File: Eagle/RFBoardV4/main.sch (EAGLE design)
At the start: 27 parts, among them Q1 8/16/20MHz, Q2 TIP41C, U1 ATMEGA328

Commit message: Added smaller mosfet - WIP
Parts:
- added Q3: (no value), transistors:2N7002_SOT23
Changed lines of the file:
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@@
 <part name="R4" library="SparkFun" deviceset="RESISTOR" device="0603-RES" value="10K"/>
 <part name="GND11" library="SparkFun" deviceset="GND" device=""/>
+<part name="Q3" library="transistors" deviceset="2N700*" device="_SOT23" technology="2"/>
 </parts>
 <sheets>
@@
 <instance part="R4" gate="G$1" x="167.64" y="172.72" rot="R180"/>
 <instance part="GND11" gate="1" x="157.48" y="175.26" rot="R180"/>
+<instance part="Q3" gate="G$1" x="93.98" y="187.96"/>
 </instances>
 <busses>

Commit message: WIP
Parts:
- removed Q2: TIP41C, transistor-power:TIP41C
- added BATMIN1, BATPLUS1: (no value), pinhead:PINHD-1X1
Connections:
- removed net SCREW_PWR: JP4.2, Q2.E
- new net SCREW_GND: JP4.1, Q3.S
- net D5: now also Q3.G; no longer Q2.B
- net GND: now also BATMIN1.1, Q3.D; no longer JP4.1
- net VCC: now also BATPLUS1.1, JP4.2; no longer Q2.C
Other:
- moved on the sheet: Q3
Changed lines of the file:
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@@
 <class number="0" name="default" width="0.1524" drill="0">
 </class>
-<class number="1" name="vcc" width="0.1524" drill="0">
+<class number="1" name="vcc" width="0.4064" drill="0">
+</class>
+<class number="2" name="GND" width="0.4064" drill="0">
 </class>
 </classes>
@@
 <part name="R3" library="SparkFun" deviceset="RESISTOR" device="0603-RES" value="10K"/>
 <part name="JP4" library="SparkFun-Connectors" deviceset="M03" device="SCREW"/>
-<part name="Q2" library="transistor-power" deviceset="TIP41C" device=""/>
 <part name="P+5" library="SparkFun" deviceset="3.3V" device="" value="VCC"/>
 <part name="GND10" library="SparkFun" deviceset="GND" device=""/>
@@
 <part name="GND11" library="SparkFun" deviceset="GND" device=""/>
 <part name="Q3" library="transistors" deviceset="2N700*" device="_SOT23" technology="2"/>
+<part name="BATMIN1" library="pinhead" deviceset="PINHD-1X1" device=""/>
+<part name="BATPLUS1" library="pinhead" deviceset="PINHD-1X1" device=""/>
+<part name="P+6" library="SparkFun" deviceset="3.3V" device="" value="VCC"/>
+<part name="GND12" library="SparkFun" deviceset="GND" device=""/>
 </parts>
 <sheets>
@@
 <instance part="R3" gate="G$1" x="30.48" y="106.68" rot="R90"/>
 <instance part="JP4" gate="G$1" x="220.98" y="187.96" rot="R180"/>
-<instance part="Q2" gate="1" x="177.8" y="185.42" rot="R90"/>
-<instance part="P+5" gate="G$1" x="165.1" y="187.96" rot="R90"/>
-<instance part="GND10" gate="1" x="200.66" y="193.04" rot="R180"/>
+<instance part="P+5" gate="G$1" x="205.74" y="187.96" rot="R90"/>
+<instance part="GND10" gate="1" x="162.56" y="193.04" rot="R180"/>
 <instance part="R4" gate="G$1" x="167.64" y="172.72" rot="R180"/>
-<instance part="GND11" gate="1" x="157.48" y="175.26" rot="R180"/>
-<instance part="Q3" gate="G$1" x="93.98" y="187.96"/>
+<instance part="GND11" gate="1" x="154.94" y="175.26" rot="R180"/>
+<instance part="Q3" gate="G$1" x="177.8" y="190.5" rot="R90"/>
+<instance part="BATMIN1" gate="G$1" x="20.32" y="154.94"/>
+<instance part="BATPLUS1" gate="G$1" x="20.32" y="170.18"/>
+<instance part="P+6" gate="G$1" x="25.4" y="170.18" rot="R270"/>
+<instance part="GND12" gate="1" x="17.78" y="147.32"/>
 </instances>
 <busses>
@@
 </segment>
 <segment>
-<pinref part="JP4" gate="G$1" pin="1"/>
-<pinref part="GND10" gate="1" pin="GND"/>
-<wire x1="213.36" y1="190.5" x2="200.66" y2="190.5" width="0.1524" layer="91"/>
-</segment>
-<segment>
 <pinref part="R4" gate="G$1" pin="2"/>
 <pinref part="GND11" gate="1" pin="GND"/>
-<wire x1="162.56" y1="172.72" x2="157.48" y2="172.72" width="0.1524" layer="91"/>
+<wire x1="162.56" y1="172.72" x2="154.94" y2="172.72" width="0.1524" layer="91"/>
+</segment>
+<segment>
+<pinref part="Q3" gate="G$1" pin="D"/>
+<pinref part="GND10" gate="1" pin="GND"/>
+<wire x1="167.64" y1="190.5" x2="162.56" y2="190.5" width="0.1524" layer="91"/>
+</segment>
+<segment>
+<pinref part="BATMIN1" gate="G$1" pin="1"/>
+<pinref part="GND12" gate="1" pin="GND"/>
+<wire x1="17.78" y1="154.94" x2="17.78" y2="149.86" width="0.1524" layer="91"/>
 </segment>
 </net>
@@
 </segment>
 <segment>
-<pinref part="Q2" gate="1" pin="C"/>
+<pinref part="JP4" gate="G$1" pin="2"/>
 <pinref part="P+5" gate="G$1" pin="3.3V"/>
-<wire x1="172.72" y1="187.96" x2="165.1" y2="187.96" width="0.1524" layer="91"/>
+<wire x1="213.36" y1="187.96" x2="205.74" y2="187.96" width="0.1524" layer="91"/>
+</segment>
+<segment>
+<pinref part="BATPLUS1" gate="G$1" pin="1"/>
+<pinref part="P+6" gate="G$1" pin="3.3V"/>
+<wire x1="17.78" y1="170.18" x2="25.4" y2="170.18" width="0.1524" layer="91"/>
 </segment>
 </net>
@@
 <pinref part="U1" gate="G$1" pin="PD5(T1)"/>
 <wire x1="195.58" y1="119.38" x2="208.28" y2="119.38" width="0.1524" layer="91"/>
-<pinref part="Q2" gate="1" pin="B"/>
-<wire x1="177.8" y1="182.88" x2="177.8" y2="172.72" width="0.1524" layer="91"/>
-<wire x1="177.8" y1="172.72" x2="177.8" y2="160.02" width="0.1524" layer="91"/>
-<wire x1="177.8" y1="160.02" x2="208.28" y2="160.02" width="0.1524" layer="91"/>
+<wire x1="180.34" y1="172.72" x2="180.34" y2="160.02" width="0.1524" layer="91"/>
+<wire x1="180.34" y1="160.02" x2="208.28" y2="160.02" width="0.1524" layer="91"/>
 <wire x1="208.28" y1="160.02" x2="208.28" y2="119.38" width="0.1524" layer="91"/>
-<junction x="177.8" y="172.72"/>
 <pinref part="R4" gate="G$1" pin="1"/>
-<wire x1="172.72" y1="172.72" x2="177.8" y2="172.72" width="0.1524" layer="91"/>
+<wire x1="172.72" y1="172.72" x2="180.34" y2="172.72" width="0.1524" layer="91"/>
+<pinref part="Q3" gate="G$1" pin="G"/>
+<wire x1="180.34" y1="180.34" x2="180.34" y2="172.72" width="0.1524" layer="91"/>
+<junction x="180.34" y="172.72"/>
 </segment>
 </net>
@@
 <wire x1="30.48" y1="101.6" x2="38.1" y2="101.6" width="0.1524" layer="91"/>
 <pinref part="R3" gate="G$1" pin="1"/>
-</segment>
-</net>
-<net name="SCREW_PWR" class="1">
-<segment>
-<pinref part="JP4" gate="G$1" pin="2"/>
-<pinref part="Q2" gate="1" pin="E"/>
-<wire x1="213.36" y1="187.96" x2="182.88" y2="187.96" width="0.1524" layer="91"/>
 </segment>
 </net>
@@
 </segment>
 </net>
+<net name="SCREW_GND" class="2">
+<segment>
+<pinref part="JP4" gate="G$1" pin="1"/>
+<pinref part="Q3" gate="G$1" pin="S"/>
+<wire x1="213.36" y1="190.5" x2="187.96" y2="190.5" width="0.1524" layer="91"/>
+</segment>
+</net>

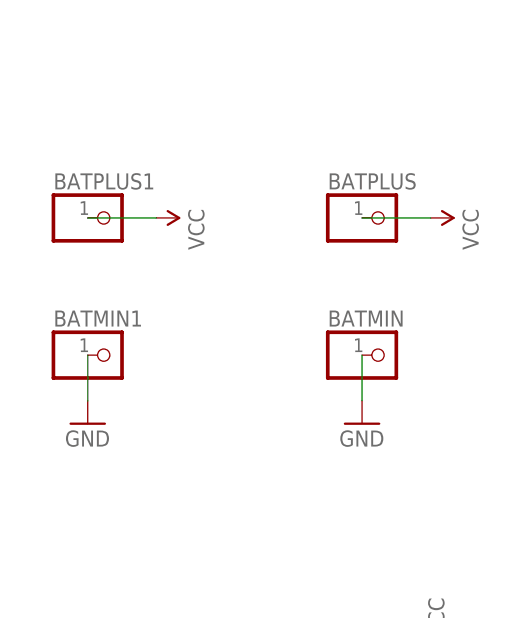
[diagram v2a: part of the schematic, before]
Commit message: V4
-Added mosfet to drive active sensors
-Added support for the X10 battery holders
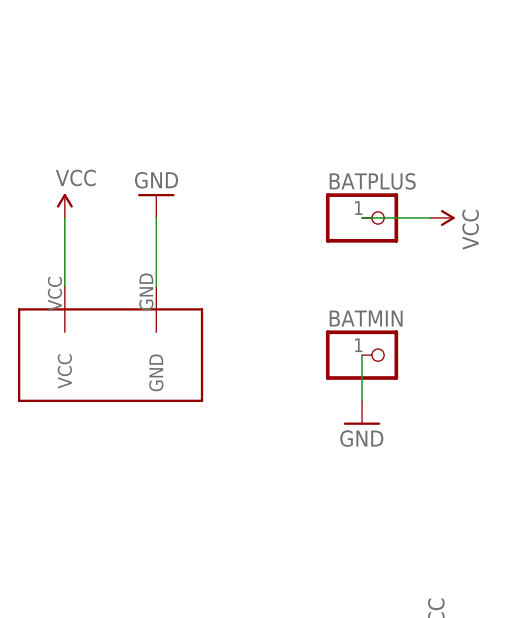
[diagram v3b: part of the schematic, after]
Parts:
- removed BATMIN1, BATPLUS1: (no value), pinhead:PINHD-1X1
- added U$1: BAT, battery_wilkie:BAT
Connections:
- net GND: now also U$1.GND; no longer BATMIN1.1
- net VCC: now also U$1.VCC; no longer BATPLUS1.1
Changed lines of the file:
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@@
 <part name="GND11" library="SparkFun" deviceset="GND" device=""/>
 <part name="Q3" library="transistors" deviceset="2N700*" device="_SOT23" technology="2"/>
-<part name="BATMIN1" library="pinhead" deviceset="PINHD-1X1" device=""/>
-<part name="BATPLUS1" library="pinhead" deviceset="PINHD-1X1" device=""/>
+<part name="U$1" library="battery_wilkie" deviceset="BAT" device=""/>
 <part name="P+6" library="SparkFun" deviceset="3.3V" device="" value="VCC"/>
 <part name="GND12" library="SparkFun" deviceset="GND" device=""/>
@@
 <instance part="GND11" gate="1" x="154.94" y="175.26" rot="R180"/>
 <instance part="Q3" gate="G$1" x="177.8" y="190.5" rot="R90"/>
-<instance part="BATMIN1" gate="G$1" x="20.32" y="154.94"/>
-<instance part="BATPLUS1" gate="G$1" x="20.32" y="170.18"/>
-<instance part="P+6" gate="G$1" x="25.4" y="170.18" rot="R270"/>
-<instance part="GND12" gate="1" x="17.78" y="147.32"/>
+<instance part="U$1" gate="G$1" x="43.18" y="147.32"/>
+<instance part="P+6" gate="G$1" x="15.24" y="170.18"/>
+<instance part="GND12" gate="1" x="25.4" y="172.72" rot="R180"/>
 </instances>
 <busses>
@@
 </segment>
 <segment>
-<pinref part="BATMIN1" gate="G$1" pin="1"/>
 <pinref part="GND12" gate="1" pin="GND"/>
-<wire x1="17.78" y1="154.94" x2="17.78" y2="149.86" width="0.1524" layer="91"/>
+<pinref part="U$1" gate="G$1" pin="GND"/>
+<wire x1="25.4" y1="170.18" x2="25.4" y2="162.56" width="0.1524" layer="91"/>
 </segment>
 </net>
@@
 </segment>
 <segment>
-<pinref part="BATPLUS1" gate="G$1" pin="1"/>
 <pinref part="P+6" gate="G$1" pin="3.3V"/>
-<wire x1="17.78" y1="170.18" x2="25.4" y2="170.18" width="0.1524" layer="91"/>
-</segment>
-</net>
+<pinref part="U$1" gate="G$1" pin="VCC"/>
+<wire x1="15.24" y1="170.18" x2="15.24" y2="162.56" width="0.1524" layer="91"/>
+</segment>
+</net>
